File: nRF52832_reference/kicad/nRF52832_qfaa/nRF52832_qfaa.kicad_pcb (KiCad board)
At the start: 2 copper layers, 45 x 40 mm, 22 parts, among them X1 32MHz, X2 32.768kHz

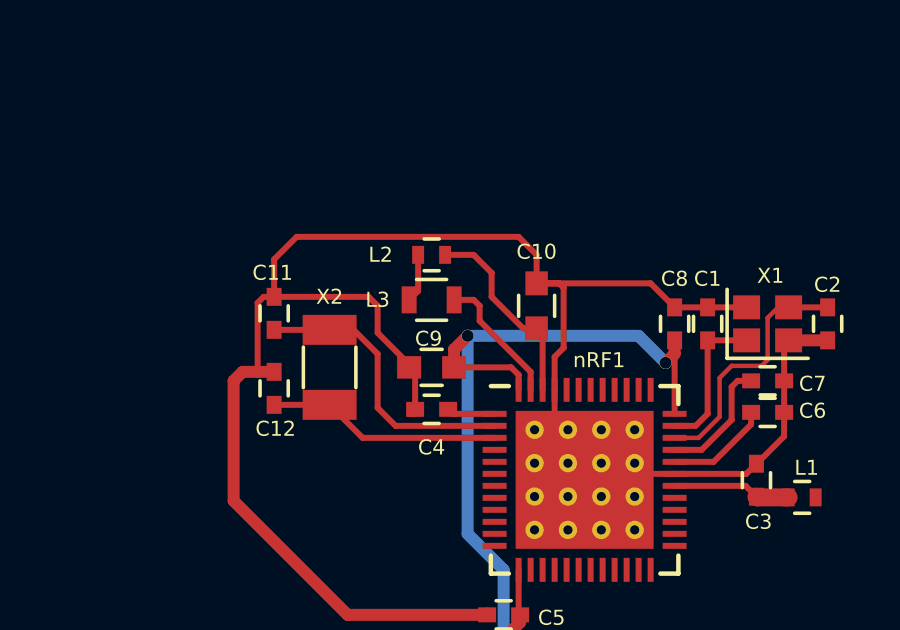
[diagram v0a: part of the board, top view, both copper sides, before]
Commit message: Reference Project nRF52832_qfaa ready
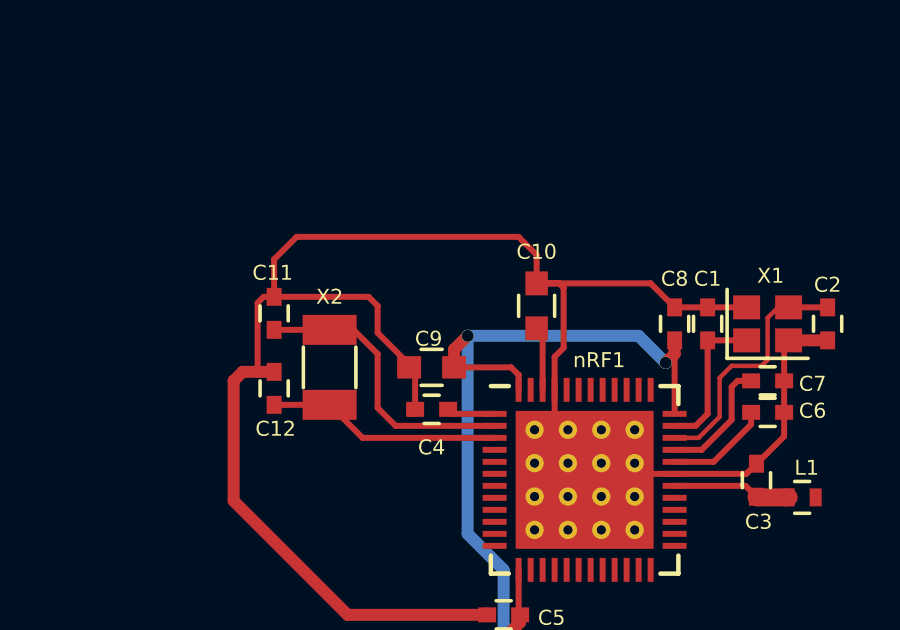
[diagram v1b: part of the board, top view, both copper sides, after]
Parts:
- removed L2: 10uH, Inductors_SMD:L_0603
- removed L3: 15nH, Inductors_SMD:L_0402
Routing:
- net Net-(nRF1-Pad47): track 4.54 -> 0.00 mm
- net /DEC4: track 6.67 -> 2.13 mm
- net Net-(L2-Pad1): track 1.62 -> 0.00 mm

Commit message: Update nRF52832_reference
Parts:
- X1: footprint Crystals:Crystal_SMD_2016-4pin_2.0x1.6mm -> Nordic_nRF:Crystal_SMD_2016-4pin_2.0x1.6mm
- X2: footprint Crystals:Crystal_SMD_3215-2pin_3.2x1.5mm -> Nordic_nRF:Crystal_SMD_3215-2pin_3.2x1.5mm
- nRF1: footprint nRF52:UQFN-48-1EP_6x6mm_Pitch0.4mm -> Nordic_nRF:Nordic_nRF-QFN40P600X600X90-48_N
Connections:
- L1 pad 2: /RF -> (no net)
